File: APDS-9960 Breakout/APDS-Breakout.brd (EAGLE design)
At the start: 53 x 80 mm, 25 parts, among them Q1 BSS138, Q2 BSS138, Q3 BSS138, U1 APDS-9960

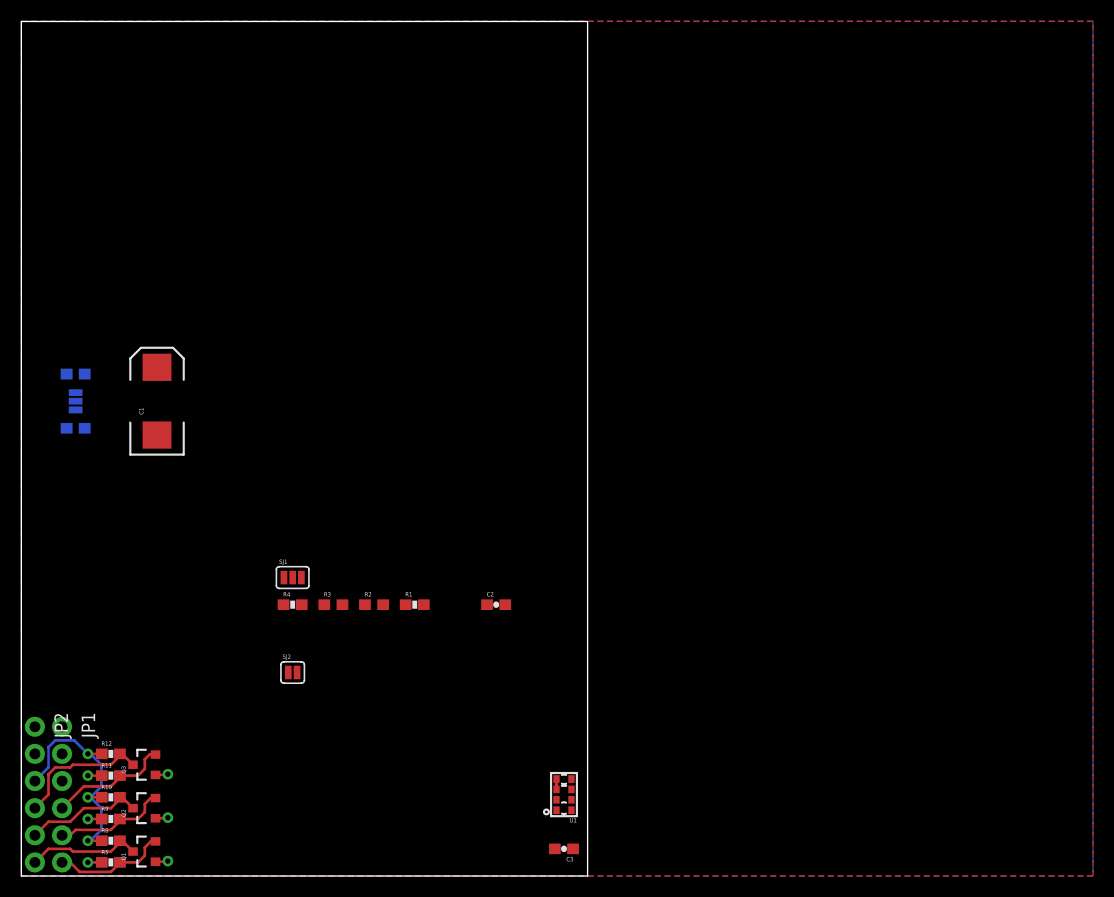
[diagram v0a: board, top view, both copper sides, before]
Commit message: Initial Design Complete
Modifications to the SparkFun design (most significant to least):
1) Rotate and relocate sensor as close as possible to edge of board.
Reason: I want to be able to put this sensor board into an enclosure
next to an LCD. The sensor needs to be as close to the LCD for both to
fit in the window.

2) Add location on back of board for large electrolytic capacitor.
Reason: placing the capacitor behind the sensor improves packaging
options for the board and sensor.

3) Added voltage regulator and level shifting components to make the
board 5V safe.
Reason: Easier to integrate with Arduinos and other 5V micros.
Note: In my understanding of the APDS datasheet the sensor can pull up
to 790mA. Because of this, a 1A regulator was selected, MCP1826T. Device
and footprint created in my Eagle library
(https://github.com/akreager/ATK_Engineering-Eagle_Library). I2C level
shifter design "borrowed" from SparkFun login level shifter board.

4) (Least important) Attempted to add provisions to be able to break
board into two pieces and reconnet with jumper wires.
Reason: Packaging.
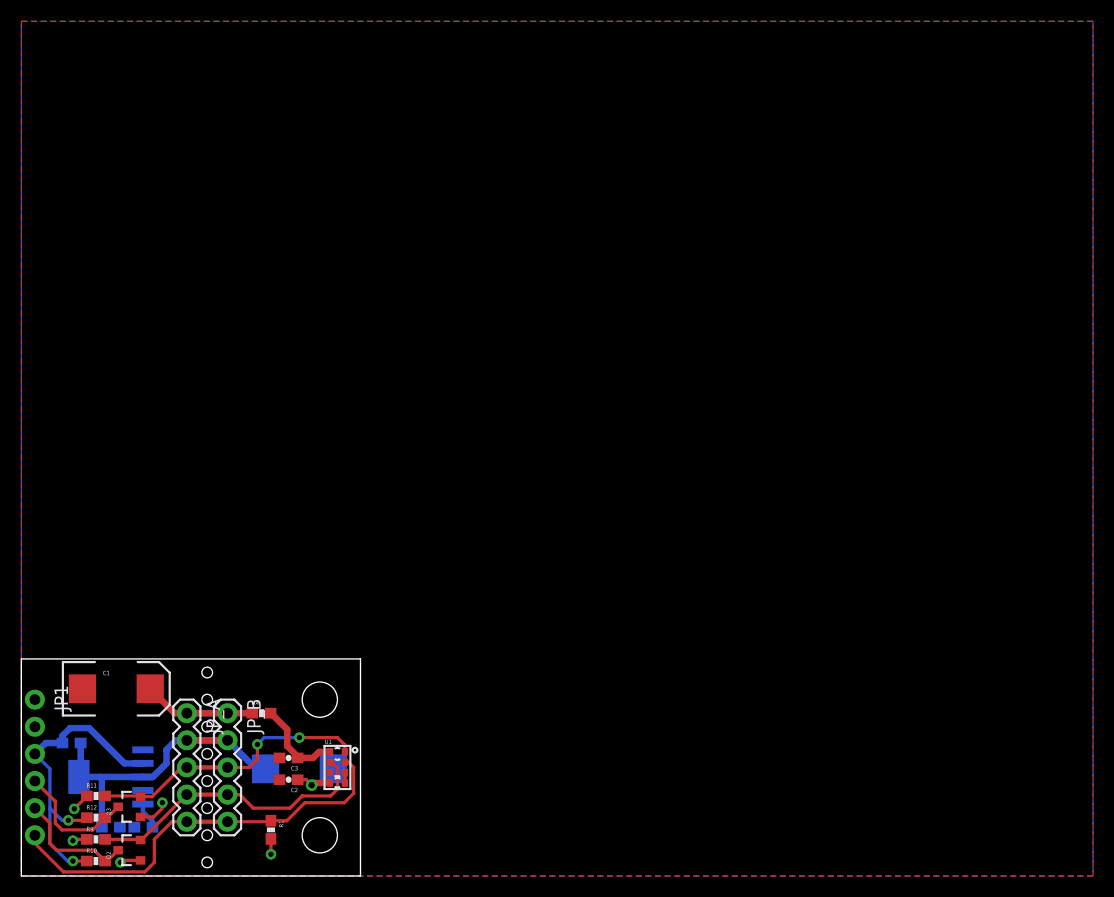
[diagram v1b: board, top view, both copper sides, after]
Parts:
- removed JP2: 5V, SparkFun-Connectors:1X06_NO_SILK
- removed Q1: BSS138, SparkFun:SOT23-3
- removed R2, R3, R7, R8: 4.7k, SparkFun-Resistors:0603
- removed R5, R6: 10K, SparkFun:0603-RES
- removed SJ1, SJ3: (no value), SparkFun-Passives:SJ_3_PASTE1&2&3
- removed SJ2: SOLDERJUMPERNC, SparkFun-Retired:SJ_2S
- added BACK_CAP: 100uF, SparkFun-Capacitors:EIA7343
- added C4: 1.0uF, SparkFun-Capacitors:0603-CAP
- added C5: 4.7uF, SparkFun-Capacitors:0603-CAP
- added JP_A, JP_B: (no value), SparkFun-Connectors:1X05
- added R13: 100K, SparkFun:0603-RES
- added U$1: MCP1826TMCP1826T, ATK_lib:SOP-223-5
- added U$2, U$3: (no value), SparkFun-Electromechanical:STAND-OFF
- JP1: value 3.3V -> 5V
- moved C1 27.2 mm to (8.89, 17.5), turned to 0 degrees
- moved C3 27.1 mm to (25.0, 11.0)
- moved C2 25.4 mm to (25.0, 9.02), turned to 180 degrees
- moved R1 25.0 mm to (23.4, 4.32), turned to 270 degrees
- moved U1 21.4 mm to (29.6, 10.2), turned to 0 degrees
- moved R4 10.6 mm to (22.5, 15.2)
- moved R10 6.13 mm to (6.99, 1.40)
- moved R12 6.13 mm to (6.99, 5.46)
- moved Q2 4.18 mm to (10.2, 2.41)
- moved Q3 4.18 mm to (10.2, 6.48)
- moved JP1 3.59 mm to (1.27, 16.5)
- moved R9 2.36 mm to (6.99, 3.43)
- moved R11 2.36 mm to (6.99, 7.49)
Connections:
- removed net INT_33: JP1.6, Q1.2, R1.1, R5.2, U1.2
- removed net INT_50: JP2.6, Q1.3, R6.2
- removed net N$2: R3.2, SJ1.1
- removed net N$3: R7.2, SJ3.3
- removed net N$5: R8.2, SJ3.1
- removed net SCL_33: JP1.5, Q2.2, R3.1, R9.2, U1.7
- removed net SCL_50: JP2.5, Q2.3, R10.2, R8.1
- removed net SDA_33: JP1.4, Q3.2, R11.2, R2.1, U1.1
- removed net SDA_50: JP2.4, Q3.3, R12.2, R7.1
- removed net VL_33: C1.A, C2.1, JP1.1, R4.1, SJ2.1, U1.5
- new net INT: JP1.6, JP_A.5, JP_B.5, R1.1, U1.2
- new net N$6: R13.2, U$1.5
- new net SCL: JP_A.4, JP_B.4, Q2.2, R9.2, U1.7
- new net SCL_5V: JP1.5, Q2.3, R10.2
- new net SDA: JP_A.3, JP_B.3, Q3.2, R11.2, U1.1
- new net SDA_5V: JP1.4, Q3.3, R12.2
- net 3.3V: now also BACK_CAP.A, C1.A, C2.1, C4.1, JP1.2, JP_A.1, JP_B.1, R13.1, R4.1, U$1.4, U1.5; no longer C3.1, JP1.3, Q1.1, R4.2, R5.1, SJ1.2, SJ2.2, U1.8
- net 5V: now also C5.2, JP1.3, U$1.2; no longer JP2.3, R6.1, SJ3.2
- net GND: now also BACK_CAP.C, C4.2, C5.1, JP1.1, JP_A.2, JP_B.2, U$1.3, U$1.6; no longer JP1.2, JP2.2
- net N$1: now also C3.1, R4.2, U1.8; no longer R2.2, SJ1.3
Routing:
- net INT: track 0.00 -> 43.4 mm
- net GND: track 0.00 -> 32.6 mm
- net SDA: track 0.00 -> 30.3 mm, vias 0 -> 2
- net SCL: track 0.00 -> 27.7 mm
- net 3.3V: track 7.48 -> 27.0 mm
- net SDA_50: track 12.9 -> 0.00 mm
- net SDA_5V: track 0.00 -> 11.8 mm
- net SDA_33: track 11.4 -> 0.00 mm
- net SCL_5V: track 0.00 -> 11.4 mm
- net SCL_50: track 11.1 -> 0.00 mm
- net INT_33: track 10.8 -> 0.00 mm
- net SCL_33: track 10.7 -> 0.00 mm
- net INT_50: track 10.7 -> 0.00 mm
- net N$1: track 0.00 -> 8.52 mm
- net 5V: track 22.7 -> 30.0 mm, vias 3 -> 2
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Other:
- board size 53 x 80 mm -> 31.8 x 20.3 mm
- board text added: "3.3V"
- board text added: "5V"
- board text added: "GND"
- board text added: "INT"
- board text added: "SCL"
- board text added: "SDA"
